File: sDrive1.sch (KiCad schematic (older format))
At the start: 0 parts

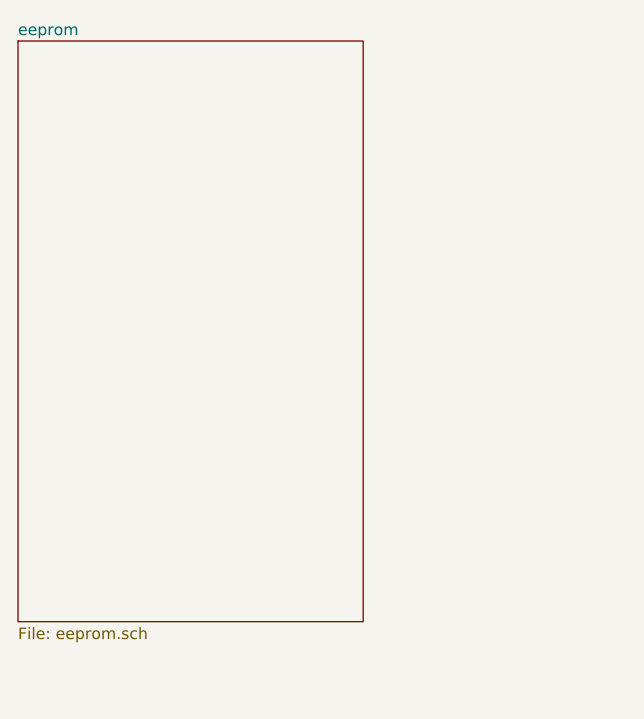
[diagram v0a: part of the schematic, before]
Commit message: update pcb layout
set board cutout
update eeprom footporint
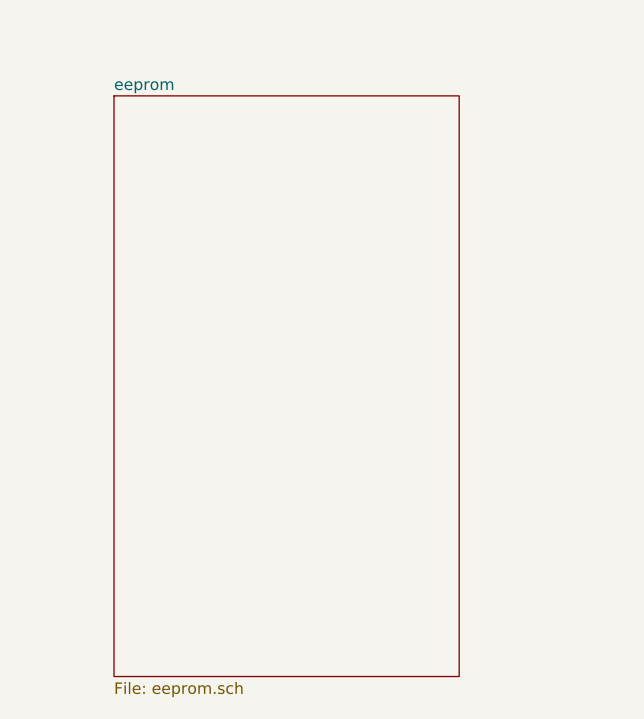
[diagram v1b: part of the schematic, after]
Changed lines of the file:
@@
 $EndSheet
 $Sheet
-S 2600 1960 1510 2540
+S 3020 2200 1510 2540
 U 60F66E2D
 F0 "eeprom" 50

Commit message: add production files
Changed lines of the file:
@@
 $EndDescr
 $Sheet
-S 8800 2050 1200 1950
+S 5500 3050 630  600
 U 60E74488
 F0 "Drive_Stage" 50
 F1 "Drive_Stage.sch" 50
+F2 "EEPROM_SDA" I L 5500 3250 50
+F3 "EEPROM_SCL" I L 5500 3350 50
+F4 "EEPROM_WP" I L 5500 3450 50
+F5 "5V" I L 5500 3550 50
 $EndSheet
 $Sheet
-S 3020 2200 1510 2540
+S 4000 3150 750  500
 U 60F66E2D
 F0 "eeprom" 50
 F1 "eeprom.sch" 50
+F2 "SCL" I R 4750 3350 50
+F3 "SDA" I R 4750 3250 50
+F4 "WP" I R 4750 3450 50
+F5 "5V_IN" I R 4750 3550 50
 $EndSheet
+Wire Wire Line
+	4750 3250 5500 3250
+Wire Wire Line
+	5500 3350 4750 3350
+Wire Wire Line
+	5500 3450 4750 3450
+Wire Wire Line
+	4750 3550 5500 3550
 $EndSCHEMATC
